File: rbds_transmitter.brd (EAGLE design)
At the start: 160 x 100 mm, 136 parts, among them J2 AVRISP-6, Q1 P-CH, Q2 P-Ch, Q3 P-Ch, T1 ATB3225-75034CT, T2 ATB3225-75034CT, U1 MAX2606, U2 TS974, U3 TS974, U4 MAX1551, U5 ATMEGA328, U6 TPS61030, U7 MCP4812, X1 16Mhz

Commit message: added value to r15, erexported
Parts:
- R15: value (none) -> 100k
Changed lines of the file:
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@@
 <element name="Q1" library="sparkfun" package="SOT23-3" value="P-CH" x="-107.95" y="105.41"/>
 <element name="D1" library="adafruit" package="SMADIODE" value="" x="-101.6" y="105.41"/>
-<element name="R15" library="adafruit" package="R1206" value="" x="-15.24" y="111.76"/>
+<element name="R15" library="adafruit" package="R1206" value="100k" x="-15.24" y="111.76"/>
 <element name="U1" library="maxim" package="SOT23-6L" value="MAX2606" x="30.48" y="66.04" rot="R270"/>
 <element name="L2" library="resistor" package="L3216C" value="485nH" x="30.48" y="69.85" rot="R180"/>

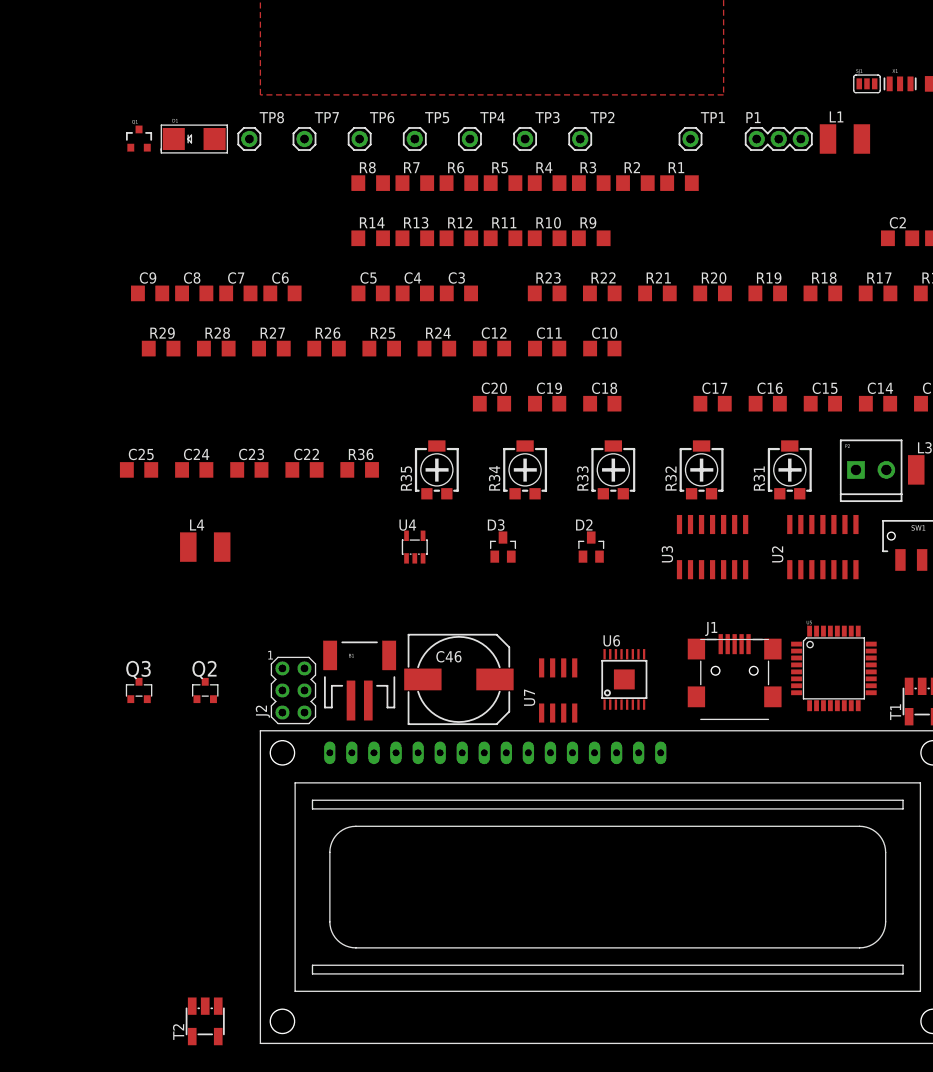
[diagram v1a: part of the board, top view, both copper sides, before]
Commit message: added bom
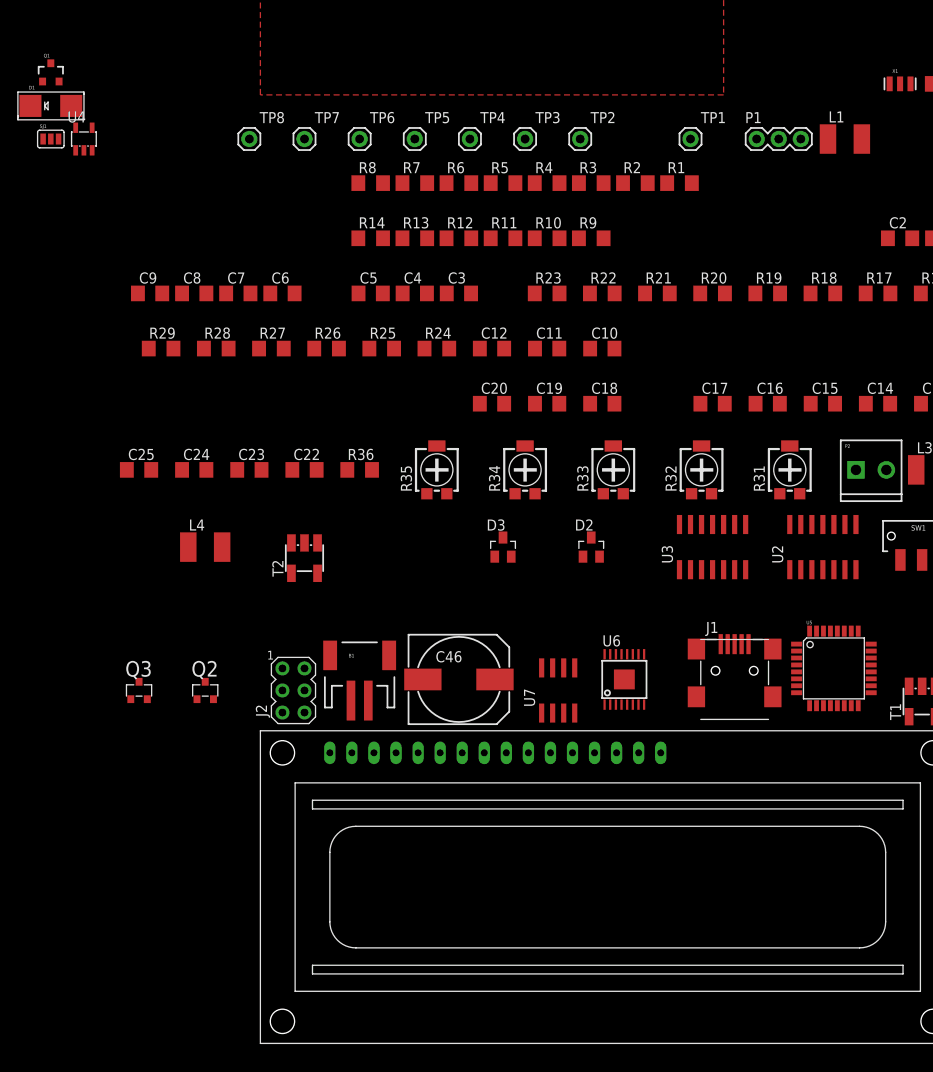
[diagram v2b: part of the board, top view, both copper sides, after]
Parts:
- moved SJ1 94.2 mm to (-118.1, 105.4)
- moved U4 60.5 mm to (-114.3, 105.4)
- moved T2 54.6 mm to (-88.9, 57.1)
- moved D1 16.9 mm to (-118.1, 109.2)
- moved Q1 12.7 mm to (-118.1, 113.0)
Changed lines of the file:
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@@
 <element name="J2" library="adafruit" package="AVRISP" value="AVRISP-6" x="-90.17" y="41.91"/>
 <element name="LCD1" library="adafruit" package="LCD1602" value="HD44780LCD-1602" x="-93.98" y="1.27"/>
-<element name="U4" library="maxim" package="SOT23-5L" value="MAX1551" x="-76.2" y="58.42">
-<attribute name="OC_NEWARK" value="88H0599" x="0" y="0" size="1.778" layer="27" display="off"/>
-<attribute name="MPN" value="MAX1551EZK-T" x="0" y="0" size="1.778" layer="27" display="off"/>
-<attribute name="MF" value="MAXIM" x="0" y="0" size="1.778" layer="27" display="off"/>
-<attribute name="OC_FARNELL" value="1628221" x="0" y="0" size="1.778" layer="27" display="off"/>
+<element name="U4" library="maxim" package="SOT23-5L" value="MAX1551" x="-114.3" y="105.41">
+<attribute name="OC_NEWARK" value="88H0599" x="-38.1" y="46.99" size="1.778" layer="27" display="off"/>
+<attribute name="MPN" value="MAX1551EZK-T" x="-38.1" y="46.99" size="1.778" layer="27" display="off"/>
+<attribute name="MF" value="MAXIM" x="-38.1" y="46.99" size="1.778" layer="27" display="off"/>
+<attribute name="OC_FARNELL" value="1628221" x="-38.1" y="46.99" size="1.778" layer="27" display="off"/>
 </element>
 <element name="C23" library="adafruit" package="C1206" value="4.7uF" x="-95.25" y="67.31"/>
@@
 <element name="B1" library="sparkfun" package="JST-2-SMD" value="" x="-82.55" y="44.45"/>
 <element name="J1" library="adafruit" package="USB-MINIB" value="" x="-39.37" y="43.18"/>
-<element name="SJ1" library="sparkfun" package="SJ_3" value="" x="-24.13" y="111.76"/>
+<element name="SJ1" library="sparkfun" package="SJ_3" value="" x="-118.11" y="105.41"/>
 <element name="Q2" library="transistor-power" package="MICRO3" value="P-Ch" x="-100.33" y="41.91"/>
 <element name="C13" library="adafruit" package="C1206" value="4.7uF" x="-16.51" y="74.93"/>
@@
 <attribute name="OC_FARNELL" value="unknown" x="0" y="0" size="1.778" layer="27" display="off"/>
 </element>
-<element name="T2" library="inductor-neosid" package="SM-T4" value="ATB3225-75034CT" x="-100.33" y="3.81">
-<attribute name="OC_NEWARK" value="unknown" x="0" y="0" size="1.778" layer="27" display="off"/>
-<attribute name="MPN" value="" x="0" y="0" size="1.778" layer="27" display="off"/>
-<attribute name="MF" value="" x="0" y="0" size="1.778" layer="27" display="off"/>
-<attribute name="OC_FARNELL" value="unknown" x="0" y="0" size="1.778" layer="27" display="off"/>
+<element name="T2" library="inductor-neosid" package="SM-T4" value="ATB3225-75034CT" x="-88.9" y="57.15">
+<attribute name="OC_NEWARK" value="unknown" x="11.43" y="53.34" size="1.778" layer="27" display="off"/>
+<attribute name="MPN" value="" x="11.43" y="53.34" size="1.778" layer="27" display="off"/>
+<attribute name="MF" value="" x="11.43" y="53.34" size="1.778" layer="27" display="off"/>
+<attribute name="OC_FARNELL" value="unknown" x="11.43" y="53.34" size="1.778" layer="27" display="off"/>
 </element>
 <element name="SW1" library="sparkfun" package="SWITCH-SPDT-SMD" value="" x="-17.78" y="59.69"/>
@@
 <element name="C19" library="adafruit" package="C1206" value="4.7uF" x="-60.96" y="74.93"/>
 <element name="C7" library="adafruit" package="C1206" value="1uF" x="-96.52" y="87.63"/>
-<element name="Q1" library="sparkfun" package="SOT23-3" value="P-CH" x="-107.95" y="105.41"/>
-<element name="D1" library="adafruit" package="SMADIODE" value="" x="-101.6" y="105.41"/>
+<element name="Q1" library="sparkfun" package="SOT23-3" value="P-CH" x="-118.11" y="113.03"/>
+<element name="D1" library="adafruit" package="SMADIODE" value="" x="-118.11" y="109.22"/>
 <element name="R15" library="adafruit" package="R1206" value="100k" x="-15.24" y="111.76"/>
 <element name="U1" library="maxim" package="SOT23-6L" value="MAX2606" x="30.48" y="66.04" rot="R270"/>
@@
 <vertex x="-93.98" y="110.49"/>
 </polygon>
-<wire x1="-100.33" y1="5.56" x2="-101.83" y2="2.06" width="0" layer="19" extent="1-1"/>
-<wire x1="-85.98" y1="34.73" x2="-100.33" y2="5.56" width="0" layer="19" extent="1-1"/>
+<wire x1="-88.9" y1="58.9" x2="-90.4" y2="55.4" width="0" layer="19" extent="1-1"/>
+<wire x1="-85.98" y1="34.73" x2="-88.9" y2="58.9" width="0" layer="19" extent="1-1"/>
 <wire x1="-88.9" y1="39.37" x2="-85.98" y2="34.73" width="0" layer="19" extent="1-1"/>
 <wire x1="-81.55" y1="40.75" x2="-85.98" y2="34.73" width="0" layer="19" extent="1-1"/>
 <wire x1="-75.27" y1="43.18" x2="-81.55" y2="40.75" width="0" layer="19" extent="1-1"/>
 <wire x1="-75.82" y1="34.73" x2="-81.55" y2="40.75" width="0" layer="19" extent="1-1"/>
-<wire x1="-76.2" y1="57.12" x2="-75.27" y2="43.18" width="0" layer="19" extent="1-1"/>
+<wire x1="-114.3" y1="104.11" x2="-75.27" y2="43.18" width="0" layer="19" extent="1-1"/>
 <wire x1="-60.325" y1="44.51" x2="-75.27" y2="43.18" width="0" layer="19" extent="1-1"/>
 <wire x1="-52.07" y1="43.18" x2="-60.325" y2="44.51" width="0" layer="19" extent="1-1"/>
@@
 <contactref element="D1" pad="A"/>
 <contactref element="L1" pad="2"/>
-<wire x1="-24.72" y1="105.41" x2="-24.13" y2="111.76" width="0" layer="19" extent="1-1"/>
-<wire x1="-99.2505" y1="105.41" x2="-24.72" y2="105.41" width="0" layer="19" extent="1-1"/>
-<wire x1="-96.65" y1="67.31" x2="-99.2505" y2="105.41" width="0" layer="19" extent="1-1"/>
+<wire x1="-24.72" y1="105.41" x2="-118.11" y2="105.41" width="0" layer="19" extent="1-1"/>
+<wire x1="-115.7605" y1="109.22" x2="-24.72" y2="105.41" width="0" layer="19" extent="1-1"/>
+<wire x1="-96.65" y1="67.31" x2="-115.7605" y2="109.22" width="0" layer="19" extent="1-1"/>
 </signal>
 <signal name="N$7">
 <contactref element="U4" pad="1"/>
 <contactref element="SJ1" pad="3"/>
-<wire x1="-77.15" y1="57.12" x2="-23.241" y2="111.76" width="0" layer="19" extent="1-1"/>
+<wire x1="-115.25" y1="104.11" x2="-117.221" y2="105.41" width="0" layer="19" extent="1-1"/>
 </signal>
 <signal name="N$8">
 <contactref element="U4" pad="4"/>
 <contactref element="SJ1" pad="1"/>
-<wire x1="-75.25" y1="59.72" x2="-25.019" y2="111.76" width="0" layer="19" extent="1-1"/>
+<wire x1="-113.35" y1="106.71" x2="-118.999" y2="105.41" width="0" layer="19" extent="1-1"/>
 </signal>
 <signal name="LCD5">
@@
 <contactref element="Q1" pad="3"/>
 <contactref element="R15" pad="1"/>
-<wire x1="-77.15" y1="59.72" x2="-16.662" y2="111.76" width="0" layer="19" extent="1-1"/>
-<wire x1="-83.55" y1="40.75" x2="-77.15" y2="59.72" width="0" layer="19" extent="1-1"/>
-<wire x1="-109.35" y1="67.31" x2="-77.15" y2="59.72" width="0" layer="19" extent="1-1"/>
-<wire x1="-107.95" y1="106.51" x2="-109.35" y2="67.31" width="0" layer="19" extent="1-1"/>
+<wire x1="-115.25" y1="106.71" x2="-16.662" y2="111.76" width="0" layer="19" extent="1-1"/>
+<wire x1="-83.55" y1="40.75" x2="-115.25" y2="106.71" width="0" layer="19" extent="1-1"/>
+<wire x1="-109.35" y1="67.31" x2="-115.25" y2="106.71" width="0" layer="19" extent="1-1"/>
+<wire x1="-118.11" y1="114.13" x2="-109.35" y2="67.31" width="0" layer="19" extent="1-1"/>
 </signal>
 <signal name="LOWBAT">
@@
 <contactref element="T2" pad="4"/>
 <contactref element="D2" pad="3"/>
-<wire x1="-55.88" y1="59.52" x2="-98.83" y2="5.56" width="0" layer="19" extent="1-1"/>
+<wire x1="-55.88" y1="59.52" x2="-87.4" y2="58.9" width="0" layer="19" extent="1-1"/>
 </signal>
 <signal name="N$14">
 <contactref element="T2" pad="2"/>
 <contactref element="D3" pad="3"/>
-<wire x1="-66.04" y1="59.52" x2="-101.83" y2="5.56" width="0" layer="19" extent="1-1"/>
+<wire x1="-66.04" y1="59.52" x2="-90.4" y2="58.9" width="0" layer="19" extent="1-1"/>
 </signal>
 <signal name="N$16">
@@
 <contactref element="U4" pad="3"/>
 <contactref element="R15" pad="2"/>
-<wire x1="-75.25" y1="57.12" x2="-13.818" y2="111.76" width="0" layer="19" extent="1-1"/>
-<wire x1="-108.9" y1="104.41" x2="-75.25" y2="57.12" width="0" layer="19" extent="1-1"/>
+<wire x1="-113.35" y1="104.11" x2="-13.818" y2="111.76" width="0" layer="19" extent="1-1"/>
+<wire x1="-119.06" y1="112.03" x2="-113.35" y2="104.11" width="0" layer="19" extent="1-1"/>
 </signal>
 <signal name="N$6">
@@
 <contactref element="Q1" pad="2"/>
 <contactref element="SW1" pad="3"/>
-<wire x1="-103.9495" y1="105.41" x2="-15.28" y2="56.94" width="0" layer="19" extent="1-1"/>
-<wire x1="-107" y1="104.41" x2="-103.9495" y2="105.41" width="0" layer="19" extent="1-1"/>
+<wire x1="-120.4595" y1="109.22" x2="-15.28" y2="56.94" width="0" layer="19" extent="1-1"/>
+<wire x1="-117.16" y1="112.03" x2="-120.4595" y2="109.22" width="0" layer="19" extent="1-1"/>
 </signal>
 <signal name="N$24">
@@
 <contactref element="T2" pad="5"/>
 <contactref element="C11" pad="1"/>
-<wire x1="-62.36" y1="81.28" x2="-98.83" y2="2.06" width="0" layer="19" extent="1-1"/>
+<wire x1="-62.36" y1="81.28" x2="-87.4" y2="55.4" width="0" layer="19" extent="1-1"/>
 </signal>
 <signal name="RBDS">

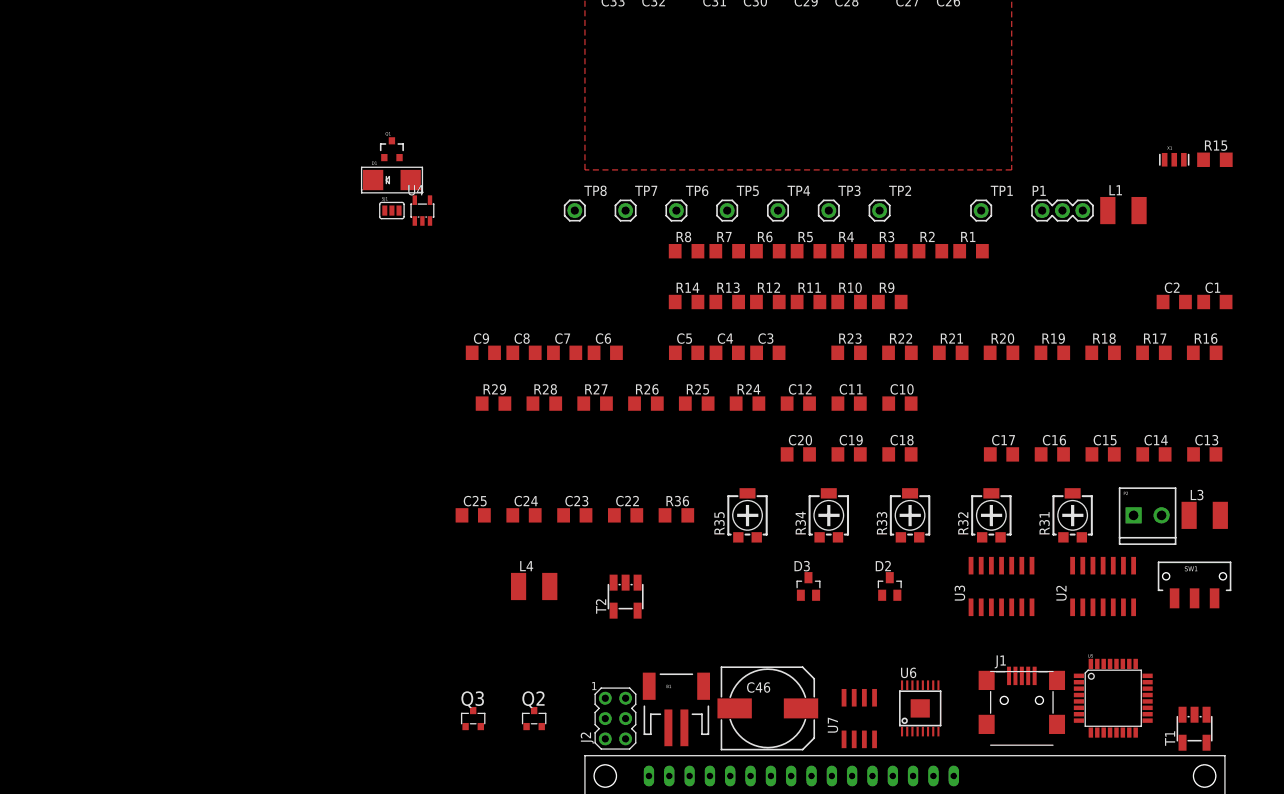
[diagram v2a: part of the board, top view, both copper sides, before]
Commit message: layed out some power components
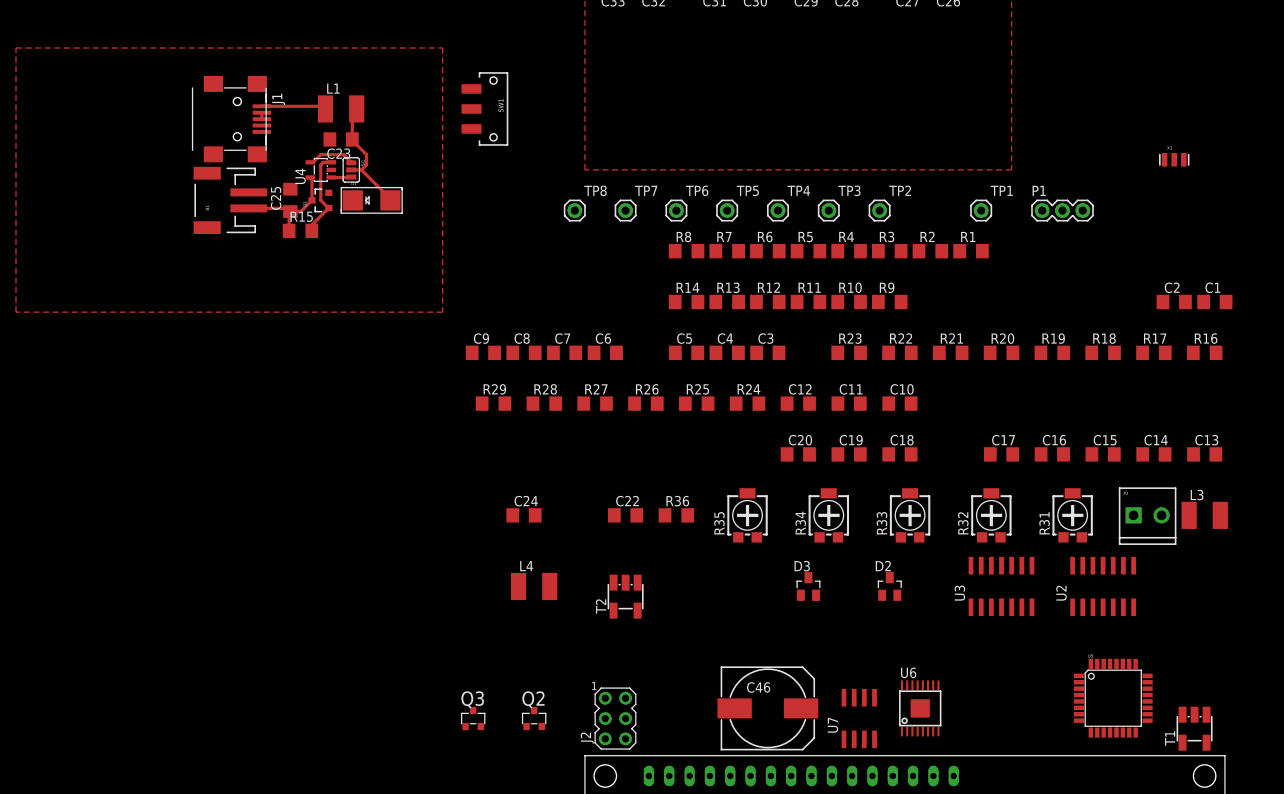
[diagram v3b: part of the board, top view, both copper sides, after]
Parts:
- moved J1 123.4 mm to (-138.4, 116.8), turned to 270 degrees
- moved R15 114.6 mm to (-129.5, 102.9)
- moved SW1 105.3 mm to (-105.4, 118.1), turned to 270 degrees
- moved L1 98.6 mm to (-124.5, 118.1)
- moved B1 84.5 mm to (-139.7, 106.7), turned to 90 degrees
- moved C23 55.3 mm to (-124.5, 114.3), turned to 180 degrees
- moved C25 45.5 mm to (-130.8, 106.7), turned to 90 degrees
- moved U4 13.7 mm to (-127.0, 110.5), turned to 90 degrees
- moved Q1 10.9 mm to (-127.0, 106.7), turned to 90 degrees
- moved SJ1 7.18 mm to (-123.2, 110.5), turned to 270 degrees
- moved D1 3.59 mm to (-120.7, 106.7)
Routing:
- net N$1: track 0.00 -> 15.6 mm
- net N$11: track 0.00 -> 14.1 mm
- net N$10: track 0.00 -> 11.2 mm
- net N$54: track 0.00 -> 8.09 mm
- net N$8: track 0.00 -> 5.96 mm
- net N$7: track 0.00 -> 2.54 mm
- net N$13: track 0.00 -> 0.80 mm

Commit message: working
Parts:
- D1: device adafruit:SMADIODE -> adafruit:SOD-123
- moved L1 39.4 mm to (-163.8, 119.4), turned to 90 degrees
- moved J1 33.0 mm to (-171.4, 115.6)
- moved B1 28.4 mm to (-167.6, 101.6), turned to 180 degrees
- moved D1 14.2 mm to (-133.3, 113.0)
- moved Q1 12.5 mm to (-138.4, 111.8)
- moved SJ1 11.1 mm to (-133.0, 105.4)
- moved C23 10.7 mm to (-130.5, 105.4), turned to 270 degrees
- moved U4 10.2 mm to (-135.9, 105.4), turned to 0 degrees
- moved R15 8.52 mm to (-133.3, 110.5), turned to 180 degrees
- moved C25 8.35 mm to (-139.1, 105.4), turned to 270 degrees
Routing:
- net N$11: track 14.1 -> 2.27 mm
- net N$10: track 11.2 -> 2.79 mm
- net N$54: track 8.09 -> 0.00 mm
- net N$1: track 15.6 -> 9.83 mm
- net N$7: track 2.54 -> 7.49 mm
- net N$8: track 5.96 -> 2.08 mm
- net N$6: track 0.00 -> 2.36 mm
- net N$13: track 0.80 -> 0.00 mm
